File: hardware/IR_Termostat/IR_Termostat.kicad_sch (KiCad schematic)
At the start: 42 parts, among them J1 USB_C_Receptacle_PowerOnly_6P, J2 JST-PH-2mm, J3 Conn_01x03_Pin, Q1 FDN306P, SW1 SW_Push_Dual, U1 TP4056-42-ESOP8, U2 XC6206P-3.3V, U4 MLX90614ESF-BAA-000-TU, U5 CH32V003JxMx, U6 DM-OLED096-636

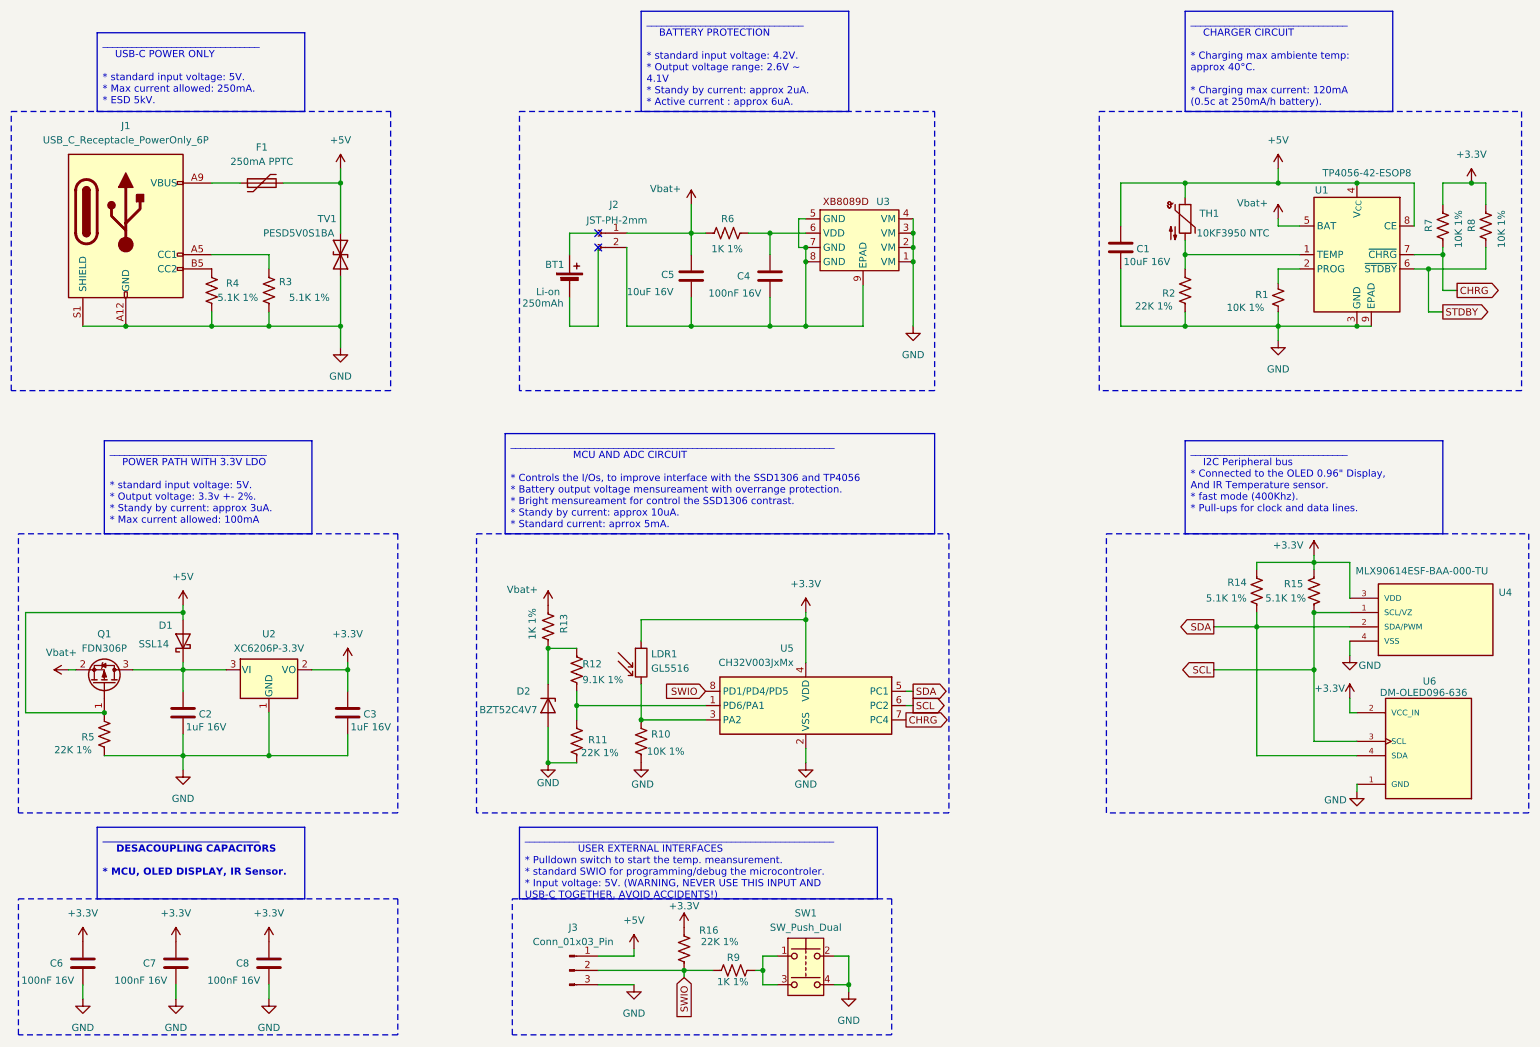
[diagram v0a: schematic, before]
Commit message: feat: initial commit on pcb branch
Actual status: Only components layout finished without their connections
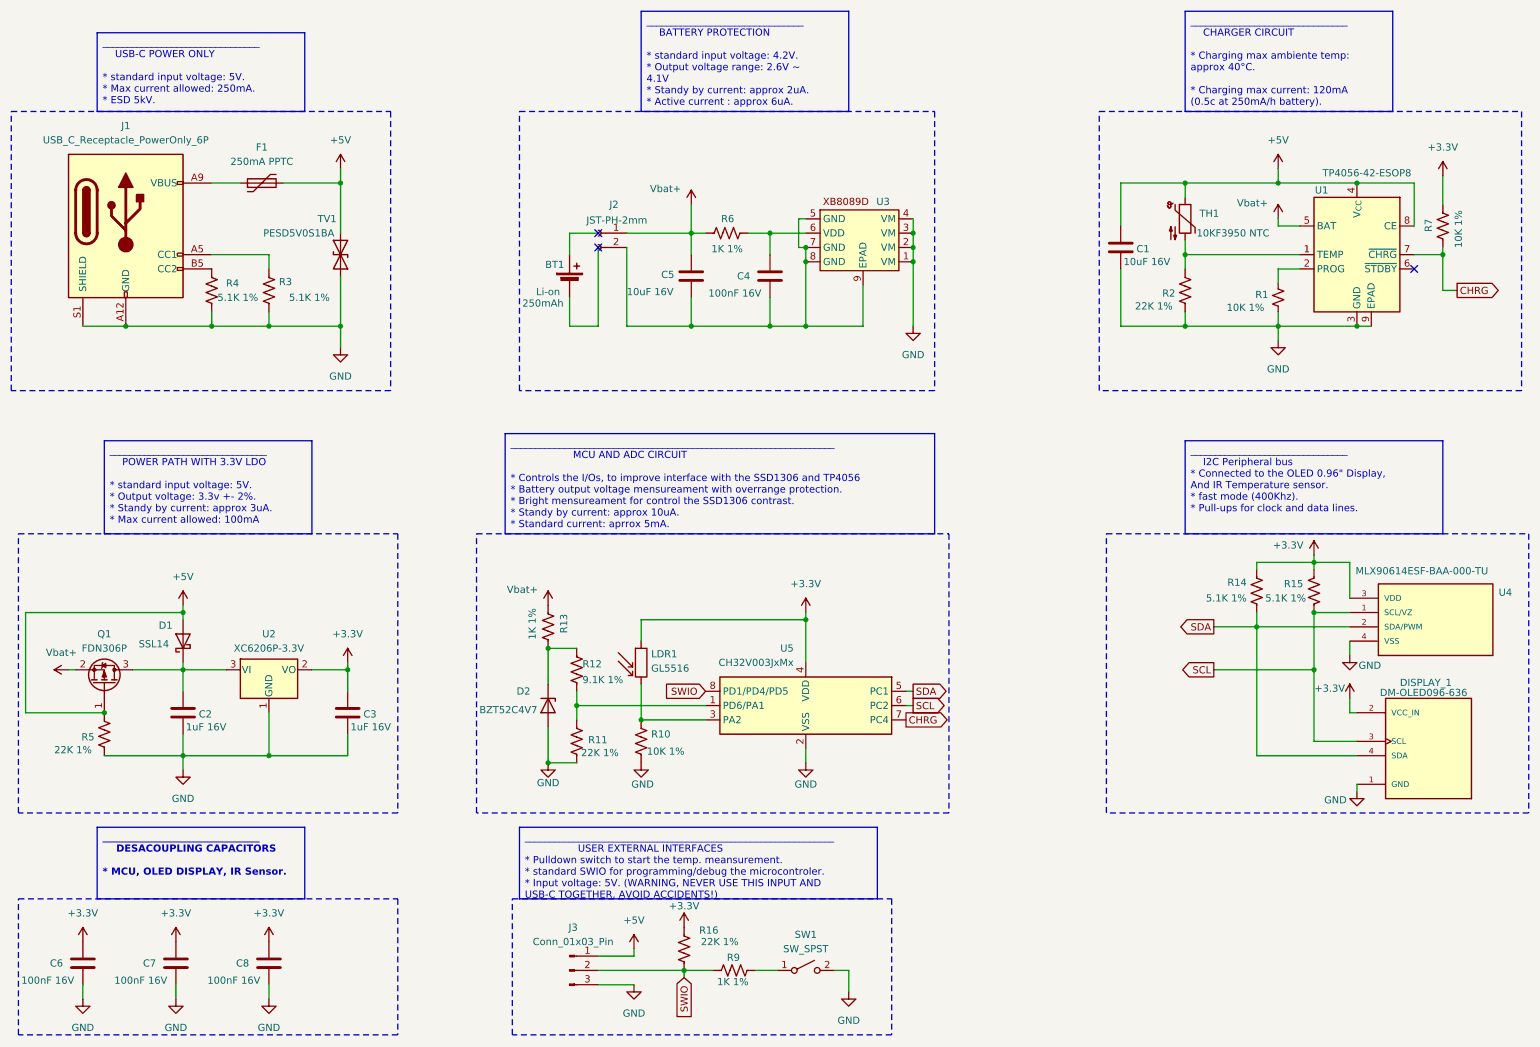
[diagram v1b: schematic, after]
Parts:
- removed R8: 10K 1%, Resistor_SMD:R_0805_2012Metric_Pad1.20x1.40mm_HandSolder, symbol Device:R_US
- removed SW1: SW_Push_Dual, Button_Switch_SMD:SW_SPST_CK_KMS2xxGP, symbol Switch:SW_Push_Dual
- added SW1: SW_SPST, Button_Switch_THT:SW_PUSH_6mm, symbol Switch:SW_SPST
- U4: footprint MLX90614ESF-BAA-000-TU:TO254P942H425-4 -> Library:TO254P942H425-4
- renumbered U6 to DISPLAY_1
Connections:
- net GND: now also SW1.2 (B)
- net at R9.2: now also SW1.1 (A)
- net STDBY: no longer names the net of U1.6 (~{STDBY})
- no-connect marks 2 -> 3
